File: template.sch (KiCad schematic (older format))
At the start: 12 parts

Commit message: Switch debouncing
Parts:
- added C? (x2): 1u, symbol Device:C
- added R? (x2): 100k, symbol Device:R
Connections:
- wire segments 39 -> 44
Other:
- moved on the sheet: SW?
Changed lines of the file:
@@
 $EndComp
-Wire Wire Line
-	7850 4300 7850 4450
-Connection ~ 7850 4450
 Wire Wire Line
 	7850 4450 7850 4500
@@
 L Switch:SW_SPST SW?
 U 1 1 6091F993
-P 3700 2100
-F 0 "SW?" H 3700 2335 50  0000 C CNN
-F 1 "bypass switch" H 3700 2244 50  0000 C CNN
-F 2 "" H 3700 2100 50  0001 C CNN
-F 3 "~" H 3700 2100 50  0001 C CNN
-	1    3700 2100
-	1    0    0    -1
-$EndComp
-Text Label 4050 2100 0    50   ~ 0
+P 8750 1300
+F 0 "SW?" H 8750 1535 50  0000 C CNN
+F 1 "bypass switch" H 8750 1444 50  0000 C CNN
+F 2 "" H 8750 1300 50  0001 C CNN
+F 3 "~" H 8750 1300 50  0001 C CNN
+	1    8750 1300
+	1    0    0    -1
+$EndComp
+Text Label 9800 1300 0    50   ~ 0
 bypass_switch
 Wire Wire Line
-	3350 2100 3500 2100
-Wire Wire Line
-	4050 2100 3900 2100
-Text Label 3350 2100 2    50   ~ 0
+	8400 1300 8550 1300
+Wire Wire Line
+	9100 1300 8950 1300
+Text Label 8400 1300 2    50   ~ 0
 5V
 $Comp
 L Switch:SW_SPST SW?
 U 1 1 60922E98
-P 3700 2500
-F 0 "SW?" H 3700 2735 50  0000 C CNN
-F 1 "preset switch" H 3700 2644 50  0000 C CNN
-F 2 "" H 3700 2500 50  0001 C CNN
-F 3 "~" H 3700 2500 50  0001 C CNN
-	1    3700 2500
-	1    0    0    -1
-$EndComp
-Text Label 4050 2500 0    50   ~ 0
+P 8750 2250
+F 0 "SW?" H 8750 2485 50  0000 C CNN
+F 1 "preset switch" H 8750 2394 50  0000 C CNN
+F 2 "" H 8750 2250 50  0001 C CNN
+F 3 "~" H 8750 2250 50  0001 C CNN
+	1    8750 2250
+	1    0    0    -1
+$EndComp
+Text Label 9800 2250 0    50   ~ 0
 preset_switch
 Wire Wire Line
-	3350 2500 3500 2500
-Wire Wire Line
-	4050 2500 3900 2500
-Text Label 3350 2500 2    50   ~ 0
+	8400 2250 8550 2250
+Wire Wire Line
+	9100 2250 8950 2250
+Text Label 8400 2250 2    50   ~ 0
 5V
 Text Label 2950 3150 0    50   ~ 0
@@
 Text Label 2700 3650 0    50   ~ 0
 rst
+$Comp
+L Device:R R?
+U 1 1 60940E91
+P 9250 1300
+F 0 "R?" V 9043 1300 50  0000 C CNN
+F 1 "100k" V 9134 1300 50  0000 C CNN
+F 2 "" V 9180 1300 50  0001 C CNN
+F 3 "~" H 9250 1300 50  0001 C CNN
+	1    9250 1300
+	0    1    1    0
+$EndComp
+$Comp
+L Device:C C?
+U 1 1 60942239
+P 9600 1550
+F 0 "C?" H 9715 1596 50  0000 L CNN
+F 1 "1u" H 9715 1505 50  0000 L CNN
+F 2 "" H 9638 1400 50  0001 C CNN
+F 3 "~" H 9600 1550 50  0001 C CNN
+	1    9600 1550
+	1    0    0    -1
+$EndComp
+$Comp
+L power:GND #PWR?
+U 1 1 60943FE3
+P 9600 1700
+F 0 "#PWR?" H 9600 1450 50  0001 C CNN
+F 1 "GND" H 9605 1527 50  0000 C CNN
+F 2 "" H 9600 1700 50  0001 C CNN
+F 3 "" H 9600 1700 50  0001 C CNN
+	1    9600 1700
+	1    0    0    -1
+$EndComp
+Wire Wire Line
+	9400 1300 9600 1300
+Wire Wire Line
+	9600 1300 9600 1400
+Connection ~ 9600 1300
+Wire Wire Line
+	9600 1300 9800 1300
+$Comp
+L Device:R R?
+U 1 1 6094831F
+P 9250 2250
+F 0 "R?" V 9043 2250 50  0000 C CNN
+F 1 "100k" V 9134 2250 50  0000 C CNN
+F 2 "" V 9180 2250 50  0001 C CNN
+F 3 "~" H 9250 2250 50  0001 C CNN
+	1    9250 2250
+	0    1    1    0
+$EndComp
+$Comp
+L Device:C C?
+U 1 1 60948325
+P 9600 2500
+F 0 "C?" H 9715 2546 50  0000 L CNN
+F 1 "1u" H 9715 2455 50  0000 L CNN
+F 2 "" H 9638 2350 50  0001 C CNN
+F 3 "~" H 9600 2500 50  0001 C CNN
+	1    9600 2500
+	1    0    0    -1
+$EndComp
+$Comp
+L power:GND #PWR?
+U 1 1 6094832B
+P 9600 2650
+F 0 "#PWR?" H 9600 2400 50  0001 C CNN
+F 1 "GND" H 9605 2477 50  0000 C CNN
+F 2 "" H 9600 2650 50  0001 C CNN
+F 3 "" H 9600 2650 50  0001 C CNN
+	1    9600 2650
+	1    0    0    -1
+$EndComp
+Wire Wire Line
+	9400 2250 9600 2250
+Wire Wire Line
+	9600 2250 9600 2350
+Connection ~ 9600 2250
+Wire Wire Line
+	9600 2250 9800 2250
 $EndSCHEMATC

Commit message: Read for review
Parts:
- removed D?: bypass LED, symbol Device:LED
- removed D?: preset LED, symbol Device:LED
- removed J?: Conn_02x03_Counter_Clockwise, symbol Connector_Generic:Conn_02x03_Counter_Clockwise
- removed Q? (x4): PN2222A, Package_TO_SOT_THT:TO-92_Inline, symbol Transistor_BJT:PN2222A
- removed R?: 100, symbol Device:R
- removed R? (x2): 100k, symbol Device:R
- removed RV?: LED brightness b1k, symbol Device:R_POT
- added C1, C3: 100n, symbol Device:C
- added C2: 100u, symbol Device:CP
- added C4: 47u, symbol Device:CP
- added D1: 1N5817, Diode_THT:D_DO-41_SOD81_P10.16mm_Horizontal, symbol Diode:1N5817
- added D2: bypass, symbol Device:LED
- added D3: preset, symbol Device:LED
- added J1: power, symbol Connector_Generic:Conn_01x02
- added J2: input, symbol Connector:AudioJack2
- added J3: output, symbol Connector:AudioJack2
- added J4: isp, symbol Connector_Generic:Conn_02x03_Odd_Even
- added K1, K2, K3: EC2-5NU, Relay_THT:Relay_DPDT_Kemet_EC2, symbol Relay:EC2-5NU
- added R1, R2: 220, symbol Device:R
- added U1: AMS1117-5.0, Package_TO_SOT_SMD:SOT-223-3_TabPin2, symbol Regulator_Linear:AMS1117-5.0
- added U3, U4: NUD3124DMT1G, Package_SO:SC-74-6_1.5x2.9mm_P0.95mm, symbol Power_Management:NUD3124DMT1G
- C5, C6: renamed from C?; value 1u -> 100n
- gave numbers to parts that had none: 3
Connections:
- net labels added: 9V, in, out, preset_1_in, preset_1_out_a, preset_1_out_b, preset_2_in, preset_2_out_a, preset_2_out_b, preset_3_in, preset_3_out_a, preset_3_out_b, relay_1, relay_2, relay_3, return, send
- net labels removed: vcc
- wire segments 44 -> 110
- no-connect marks 0 -> 3
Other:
- moved on the sheet: SW1, SW2, U2

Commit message: whoops
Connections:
- net 9V: now also C2.1, D1.1 (K)
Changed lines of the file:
@@
 Wire Wire Line
 	1350 2400 1350 2350
+Text GLabel 2350 950  2    50   Input ~ 0
+9V
+Wire Wire Line
+	2350 950  2200 950
+Connection ~ 2200 950
 $EndSCHEMATC

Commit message: Fix a few values
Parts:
- removed C2: 100u, symbol Device:CP
- removed C4: 47u, symbol Device:CP
- added C? (x2): 10u, symbol Device:C
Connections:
- net 5V: now also C?.1; no longer SW1.1 (A), SW2.1 (A)
- net 9V: now also C?.1
- net GND: now also SW1.1 (A), SW2.1 (A), C?.2, C?.2
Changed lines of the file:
@@
 Wire Wire Line
 	8850 1300 9000 1300
-Text Label 8850 1300 2    50   ~ 0
-5V
 $Comp
 L Switch:SW_SPST SW2
@@
 Wire Wire Line
 	8850 2250 9000 2250
-Text Label 8850 2250 2    50   ~ 0
-5V
 Text Label 4950 3150 0    50   ~ 0
 bypass_switch
@@
 $EndComp
 $Comp
-L Device:CP C2
-U 1 1 60D34350
-P 2200 1200
-F 0 "C2" H 2318 1246 50  0000 L CNN
-F 1 "100u" H 2318 1155 50  0000 L CNN
-F 2 "" H 2238 1050 50  0001 C CNN
-F 3 "~" H 2200 1200 50  0001 C CNN
-	1    2200 1200
-	1    0    0    -1
-$EndComp
-$Comp
 L power:GND #PWR05
 U 1 1 60D34D4F
@@
 	2200 950  2200 1050
 $Comp
-L Device:CP C4
-U 1 1 60D3F51B
-P 3050 2700
-F 0 "C4" H 3168 2746 50  0000 L CNN
-F 1 "47u" H 3168 2655 50  0000 L CNN
-F 2 "" H 3088 2550 50  0001 C CNN
-F 3 "~" H 3050 2700 50  0001 C CNN
-	1    3050 2700
-	1    0    0    -1
-$EndComp
-$Comp
 L Device:C C3
 U 1 1 60D400E3
@@
 	2350 950  2200 950
 Connection ~ 2200 950
+$Comp
+L power:GND #PWR?
+U 1 1 60E185E6
+P 8850 1400
+F 0 "#PWR?" H 8850 1150 50  0001 C CNN
+F 1 "GND" H 8855 1227 50  0000 C CNN
+F 2 "" H 8850 1400 50  0001 C CNN
+F 3 "" H 8850 1400 50  0001 C CNN
+	1    8850 1400
+	1    0    0    -1
+$EndComp
+Wire Wire Line
+	8850 1400 8850 1300
+$Comp
+L power:GND #PWR?
+U 1 1 60E1D76B
+P 8850 2350
+F 0 "#PWR?" H 8850 2100 50  0001 C CNN
+F 1 "GND" H 8855 2177 50  0000 C CNN
+F 2 "" H 8850 2350 50  0001 C CNN
+F 3 "" H 8850 2350 50  0001 C CNN
+	1    8850 2350
+	1    0    0    -1
+$EndComp
+Wire Wire Line
+	8850 2350 8850 2250
+$Comp
+L Device:C C?
+U 1 1 60E28EBF
+P 3050 2700
+F 0 "C?" H 3165 2746 50  0000 L CNN
+F 1 "10u" H 3165 2655 50  0000 L CNN
+F 2 "" H 3088 2550 50  0001 C CNN
+F 3 "~" H 3050 2700 50  0001 C CNN
+	1    3050 2700
+	1    0    0    -1
+$EndComp
+$Comp
+L Device:C C?
+U 1 1 60E30D9E
+P 2200 1200
+F 0 "C?" H 2315 1246 50  0000 L CNN
+F 1 "10u" H 2315 1155 50  0000 L CNN
+F 2 "" H 2238 1050 50  0001 C CNN
+F 3 "~" H 2200 1200 50  0001 C CNN
+	1    2200 1200
+	1    0    0    -1
+$EndComp
 $EndSCHEMATC

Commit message: Now with an input buffer to preserve phase
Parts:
- gave numbers to parts that had none: 2
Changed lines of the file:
@@
 $EndComp
 $Comp
-L power:GND #PWR015
+L power:GND #PWR017
 U 1 1 60943FE3
 P 9600 1700
-F 0 "#PWR015" H 9600 1450 50  0001 C CNN
+F 0 "#PWR017" H 9600 1450 50  0001 C CNN
 F 1 "GND" H 9605 1527 50  0000 C CNN
 F 2 "" H 9600 1700 50  0001 C CNN
@@
 $EndComp
 $Comp
-L power:GND #PWR016
+L power:GND #PWR018
 U 1 1 6094832B
 P 9600 2650
-F 0 "#PWR016" H 9600 2400 50  0001 C CNN
+F 0 "#PWR018" H 9600 2400 50  0001 C CNN
 F 1 "GND" H 9605 2477 50  0000 C CNN
 F 2 "" H 9600 2650 50  0001 C CNN
@@
 Connection ~ 2200 950
 $Comp
-L power:GND #PWR?
+L power:GND #PWR015
 U 1 1 60E185E6
 P 8850 1400
-F 0 "#PWR?" H 8850 1150 50  0001 C CNN
+F 0 "#PWR015" H 8850 1150 50  0001 C CNN
 F 1 "GND" H 8855 1227 50  0000 C CNN
 F 2 "" H 8850 1400 50  0001 C CNN
@@
 	8850 1400 8850 1300
 $Comp
-L power:GND #PWR?
+L power:GND #PWR016
 U 1 1 60E1D76B
 P 8850 2350
-F 0 "#PWR?" H 8850 2100 50  0001 C CNN
+F 0 "#PWR016" H 8850 2100 50  0001 C CNN
 F 1 "GND" H 8855 2177 50  0000 C CNN
 F 2 "" H 8850 2350 50  0001 C CNN
@@
 	8850 2350 8850 2250
 $Comp
-L Device:C C?
+L Device:C C4
 U 1 1 60E28EBF
 P 3050 2700
-F 0 "C?" H 3165 2746 50  0000 L CNN
+F 0 "C4" H 3165 2746 50  0000 L CNN
 F 1 "10u" H 3165 2655 50  0000 L CNN
 F 2 "" H 3088 2550 50  0001 C CNN
@@
 $EndComp
 $Comp
-L Device:C C?
+L Device:C C2
 U 1 1 60E30D9E
 P 2200 1200
-F 0 "C?" H 2315 1246 50  0000 L CNN
+F 0 "C2" H 2315 1246 50  0000 L CNN
 F 1 "10u" H 2315 1155 50  0000 L CNN
 F 2 "" H 2238 1050 50  0001 C CNN

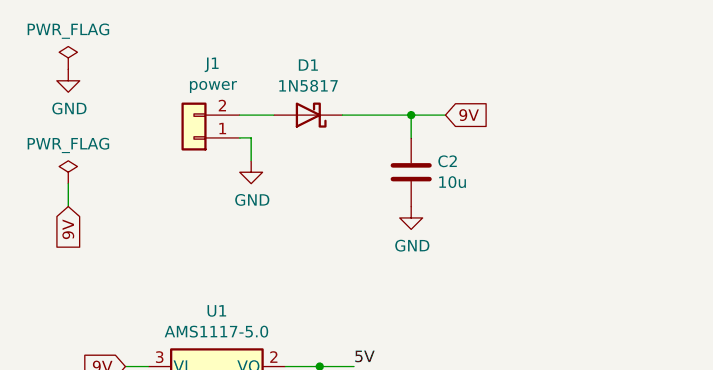
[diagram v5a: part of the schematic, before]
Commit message: Add resistor footprints/part numbers
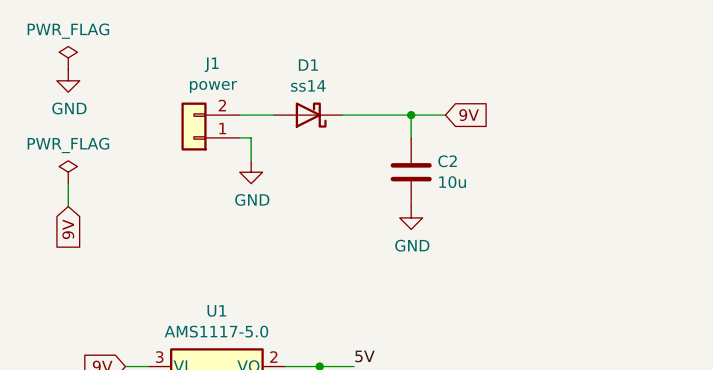
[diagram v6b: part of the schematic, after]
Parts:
- removed D1: 1N5817, Diode_THT:D_DO-41_SOD81_P10.16mm_Horizontal, symbol Diode:1N5817
- added D1: ss14, Diode_SMD:D_SMA, symbol Device:D_Schottky
- R1, R2: footprint (none) -> Resistor_SMD:R_0603_1608Metric; LCSC (none) -> C22962
- SW1, SW2: footprint (none) -> Connector_JST:JST_XH_B2B-XH-AM_1x02_P2.50mm_Vertical
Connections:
- net 9V: now also D1.1 (K)
- net at J1.2 (Pin_2): now also D1.2 (A)
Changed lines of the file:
@@
 F 0 "SW1" H 9200 1535 50  0000 C CNN
 F 1 "bypass switch" H 9200 1444 50  0000 C CNN
-F 2 "" H 9200 1300 50  0001 C CNN
+F 2 "Connector_JST:JST_XH_B2B-XH-AM_1x02_P2.50mm_Vertical" H 9200 1300 50  0001 C CNN
 F 3 "~" H 9200 1300 50  0001 C CNN
 	1    9200 1300
@@
 F 0 "SW2" H 9200 2485 50  0000 C CNN
 F 1 "preset switch" H 9200 2394 50  0000 C CNN
-F 2 "" H 9200 2250 50  0001 C CNN
+F 2 "Connector_JST:JST_XH_B2B-XH-AM_1x02_P2.50mm_Vertical" H 9200 2250 50  0001 C CNN
 F 3 "~" H 9200 2250 50  0001 C CNN
 	1    9200 2250
@@
 F 0 "R1" V 7393 1300 50  0000 C CNN
 F 1 "220" V 7484 1300 50  0000 C CNN
-F 2 "" V 7530 1300 50  0001 C CNN
+F 2 "Resistor_SMD:R_0603_1608Metric" V 7530 1300 50  0001 C CNN
 F 3 "~" H 7600 1300 50  0001 C CNN
+F 4 "C22962" V 7600 1300 50  0001 C CNN "LCSC"
 	1    7600 1300
 	0    1    1    0
@@
 F 0 "R2" V 7393 2250 50  0000 C CNN
 F 1 "220" V 7484 2250 50  0000 C CNN
-F 2 "" V 7530 2250 50  0001 C CNN
+F 2 "Resistor_SMD:R_0603_1608Metric" V 7530 2250 50  0001 C CNN
 F 3 "~" H 7600 2250 50  0001 C CNN
+F 4 "C22962" V 7600 2250 50  0001 C CNN "LCSC"
 	1    7600 2250
 	0    1    1    0
@@
 	700  1350 700  1250
 $Comp
-L Diode:1N5817 D1
-U 1 1 60D32E89
-P 1750 950
-F 0 "D1" H 1750 733 50  0000 C CNN
-F 1 "1N5817" H 1750 824 50  0000 C CNN
-F 2 "Diode_THT:D_DO-41_SOD81_P10.16mm_Horizontal" H 1750 775 50  0001 C CNN
-F 3 "http://www.vishay.com/docs/88525/1n5817.pdf" H 1750 950 50  0001 C CNN
-	1    1750 950
-	-1   0    0    1
-$EndComp
-$Comp
 L power:GND #PWR05
 U 1 1 60D34D4F
@@
 	1    0    0    -1
 $EndComp
+$Comp
+L Device:D_Schottky D1
+U 1 1 60EE548D
+P 1750 950
+F 0 "D1" H 1750 733 50  0000 C CNN
+F 1 "ss14" H 1750 824 50  0000 C CNN
+F 2 "Diode_SMD:D_SMA" H 1750 950 50  0001 C CNN
+F 3 "~" H 1750 950 50  0001 C CNN
+F 4 "C2480" H 1750 950 50  0001 C CNN "LCSC"
+	1    1750 950
+	-1   0    0    1
+$EndComp
 $EndSCHEMATC

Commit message: Capacitors
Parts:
- C1, C3, C5, C6: footprint (none) -> Capacitor_SMD:C_0603_1608Metric; LCSC (none) -> C14663
- C2, C4: footprint (none) -> Capacitor_SMD:C_1206_3216Metric; LCSC (none) -> C13585
- D2, D3: footprint (none) -> LED_THT:LED_D5.0mm
- J1: footprint (none) -> Connector_PinHeader_2.54mm:PinHeader_1x02_P2.54mm_Vertical
- J4: footprint (none) -> Connector_PinHeader_2.54mm:PinHeader_2x03_P2.54mm_Vertical
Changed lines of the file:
@@
 F 0 "C5" H 9715 1596 50  0000 L CNN
 F 1 "100n" H 9715 1505 50  0000 L CNN
-F 2 "" H 9638 1400 50  0001 C CNN
+F 2 "Capacitor_SMD:C_0603_1608Metric" H 9638 1400 50  0001 C CNN
 F 3 "~" H 9600 1550 50  0001 C CNN
+F 4 "C14663" H 9600 1550 50  0001 C CNN "LCSC"
 	1    9600 1550
 	1    0    0    -1
@@
 F 0 "C6" H 9715 2546 50  0000 L CNN
 F 1 "100n" H 9715 2455 50  0000 L CNN
-F 2 "" H 9638 2350 50  0001 C CNN
+F 2 "Capacitor_SMD:C_0603_1608Metric" H 9638 2350 50  0001 C CNN
 F 3 "~" H 9600 2500 50  0001 C CNN
+F 4 "C14663" H 9600 2500 50  0001 C CNN "LCSC"
 	1    9600 2500
 	1    0    0    -1
@@
 F 0 "D2" H 8043 1045 50  0000 C CNN
 F 1 "bypass" H 8043 1136 50  0000 C CNN
-F 2 "" H 8050 1300 50  0001 C CNN
+F 2 "LED_THT:LED_D5.0mm" H 8050 1300 50  0001 C CNN
 F 3 "~" H 8050 1300 50  0001 C CNN
 	1    8050 1300
@@
 F 0 "D3" H 8043 1995 50  0000 C CNN
 F 1 "preset" H 8043 2086 50  0000 C CNN
-F 2 "" H 8050 2250 50  0001 C CNN
+F 2 "LED_THT:LED_D5.0mm" H 8050 2250 50  0001 C CNN
 F 3 "~" H 8050 2250 50  0001 C CNN
 	1    8050 2250
@@
 F 0 "J1" H 1168 725 50  0000 C CNN
 F 1 "power" H 1168 816 50  0000 C CNN
-F 2 "" H 1250 1050 50  0001 C CNN
+F 2 "Connector_PinHeader_2.54mm:PinHeader_1x02_P2.54mm_Vertical" H 1250 1050 50  0001 C CNN
 F 3 "~" H 1250 1050 50  0001 C CNN
 	1    1250 1050
@@
 F 0 "J4" H 6450 4217 50  0000 C CNN
 F 1 "isp" H 6450 4126 50  0000 C CNN
-F 2 "" H 6400 3900 50  0001 C CNN
+F 2 "Connector_PinHeader_2.54mm:PinHeader_2x03_P2.54mm_Vertical" H 6400 3900 50  0001 C CNN
 F 3 "~" H 6400 3900 50  0001 C CNN
 	1    6400 3900
@@
 F 0 "C3" H 2715 2746 50  0000 L CNN
 F 1 "100n" H 2715 2655 50  0000 L CNN
-F 2 "" H 2638 2550 50  0001 C CNN
+F 2 "Capacitor_SMD:C_0603_1608Metric" H 2638 2550 50  0001 C CNN
 F 3 "~" H 2600 2700 50  0001 C CNN
+F 4 "C14663" H 2600 2700 50  0001 C CNN "LCSC"
 	1    2600 2700
 	1    0    0    -1
@@
 F 0 "C1" H 1915 2296 50  0000 L CNN
 F 1 "100n" H 1915 2205 50  0000 L CNN
-F 2 "" H 1838 2100 50  0001 C CNN
+F 2 "Capacitor_SMD:C_0603_1608Metric" H 1838 2100 50  0001 C CNN
 F 3 "~" H 1800 2250 50  0001 C CNN
+F 4 "C14663" H 1800 2250 50  0001 C CNN "LCSC"
 	1    1800 2250
 	1    0    0    -1
@@
 F 0 "C4" H 3165 2746 50  0000 L CNN
 F 1 "10u" H 3165 2655 50  0000 L CNN
-F 2 "" H 3088 2550 50  0001 C CNN
+F 2 "Capacitor_SMD:C_1206_3216Metric" H 3088 2550 50  0001 C CNN
 F 3 "~" H 3050 2700 50  0001 C CNN
+F 4 "C13585" H 3050 2700 50  0001 C CNN "LCSC"
 	1    3050 2700
 	1    0    0    -1
@@
 F 0 "C2" H 2315 1246 50  0000 L CNN
 F 1 "10u" H 2315 1155 50  0000 L CNN
-F 2 "" H 2238 1050 50  0001 C CNN
+F 2 "Capacitor_SMD:C_1206_3216Metric" H 2238 1050 50  0001 C CNN
 F 3 "~" H 2200 1200 50  0001 C CNN
+F 4 "C13585" H 2200 1200 50  0001 C CNN "LCSC"
 	1    2200 1200
 	1    0    0    -1

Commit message: Everything except those damn pots
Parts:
- removed U2: ATtiny85-20PU, Package_DIP:DIP-8_W7.62mm, symbol MCU_Microchip_ATtiny:ATtiny85-20PU
- added U2: ATtiny85-20SU, Package_SO:SOIJ-8_5.3x5.3mm_P1.27mm, symbol MCU_Microchip_ATtiny:ATtiny85-20SU
- J2, J3: footprint (none) -> Connector_Audio:Jack_6.35mm_Neutrik_NMJ4HCD2_Horizontal
- U1: LCSC (none) -> C6187
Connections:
- net 5V: now also U2.8 (VCC)
- net GND: now also U2.4 (GND)
- net bypass_led: now also U2.7 (PB2)
- net bypass_relay: now also U2.2 (XTAL1/PB3)
- net bypass_switch: now also U2.5 (AREF/PB0)
- net miso: now also U2.6 (PB1)
- net preset_relay: now also U2.3 (XTAL2/PB4)
- net rst: now also U2.1 (~RESET~/PB5)
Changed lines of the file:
@@
 $EndDescr
-$Comp
-L MCU_Microchip_ATtiny:ATtiny85-20PU U2
-U 1 1 60917AD6
-P 4000 3450
-F 0 "U2" H 3471 3496 50  0000 R CNN
-F 1 "ATtiny85-20PU" H 3471 3405 50  0000 R CNN
-F 2 "Package_DIP:DIP-8_W7.62mm" H 4000 3450 50  0001 C CIN
-F 3 "http://ww1.microchip.com/downloads/en/DeviceDoc/atmel-2586-avr-8-bit-microcontroller-attiny25-attiny45-attiny85_datasheet.pdf" H 4000 3450 50  0001 C CNN
-	1    4000 3450
-	1    0    0    -1
-$EndComp
 $Comp
 L power:GND #PWR07
@@
 F 0 "J2" H 3900 1500 50  0000 C CNN
 F 1 "input" H 3900 1400 50  0000 C CNN
-F 2 "" H 3900 1150 50  0001 C CNN
+F 2 "Connector_Audio:Jack_6.35mm_Neutrik_NMJ4HCD2_Horizontal" H 3900 1150 50  0001 C CNN
 F 3 "~" H 3900 1150 50  0001 C CNN
 	1    3900 1150
@@
 F 0 "J3" H 4650 1500 50  0000 C CNN
 F 1 "output" H 4650 1400 50  0000 C CNN
-F 2 "" H 4650 1150 50  0001 C CNN
+F 2 "Connector_Audio:Jack_6.35mm_Neutrik_NMJ4HCD2_Horizontal" H 4650 1150 50  0001 C CNN
 F 3 "~" H 4650 1150 50  0001 C CNN
 	1    4650 1150
@@
 F 2 "Package_TO_SOT_SMD:SOT-223-3_TabPin2" H 1350 2250 50  0001 C CNN
 F 3 "http://www.advanced-monolithic.com/pdf/ds1117.pdf" H 1450 1800 50  0001 C CNN
+F 4 "C6187" H 1350 2050 50  0001 C CNN "LCSC"
 	1    1350 2050
 	1    0    0    -1
@@
 	-1   0    0    1
 $EndComp
+$Comp
+L MCU_Microchip_ATtiny:ATtiny85-20SU U2
+U 1 1 60FD1067
+P 4000 3450
+F 0 "U2" H 3471 3496 50  0000 R CNN
+F 1 "ATtiny85-20SU" H 3471 3405 50  0000 R CNN
+F 2 "Package_SO:SOIJ-8_5.3x5.3mm_P1.27mm" H 4000 3450 50  0001 C CIN
+F 3 "http://ww1.microchip.com/downloads/en/DeviceDoc/atmel-2586-avr-8-bit-microcontroller-attiny25-attiny45-attiny85_datasheet.pdf" H 4000 3450 50  0001 C CNN
+	1    4000 3450
+	1    0    0    -1
+$EndComp
 $EndSCHEMATC
